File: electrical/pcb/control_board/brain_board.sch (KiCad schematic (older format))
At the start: 6 parts

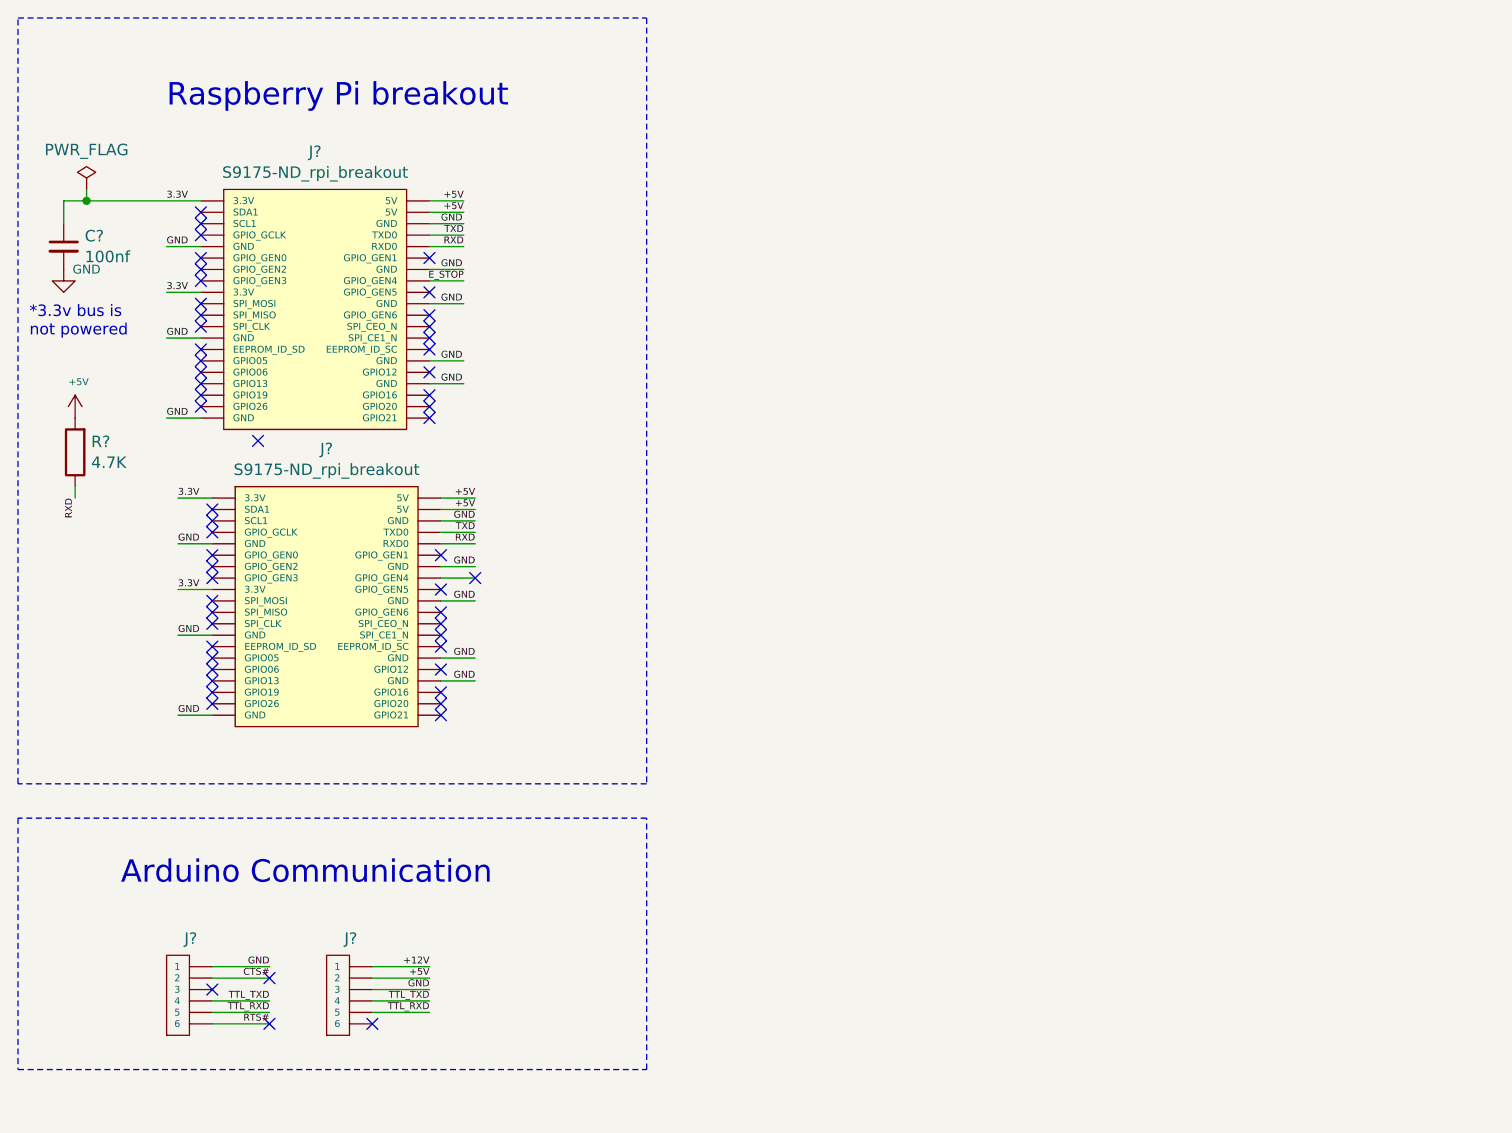
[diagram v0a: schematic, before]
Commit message: add inter board connector
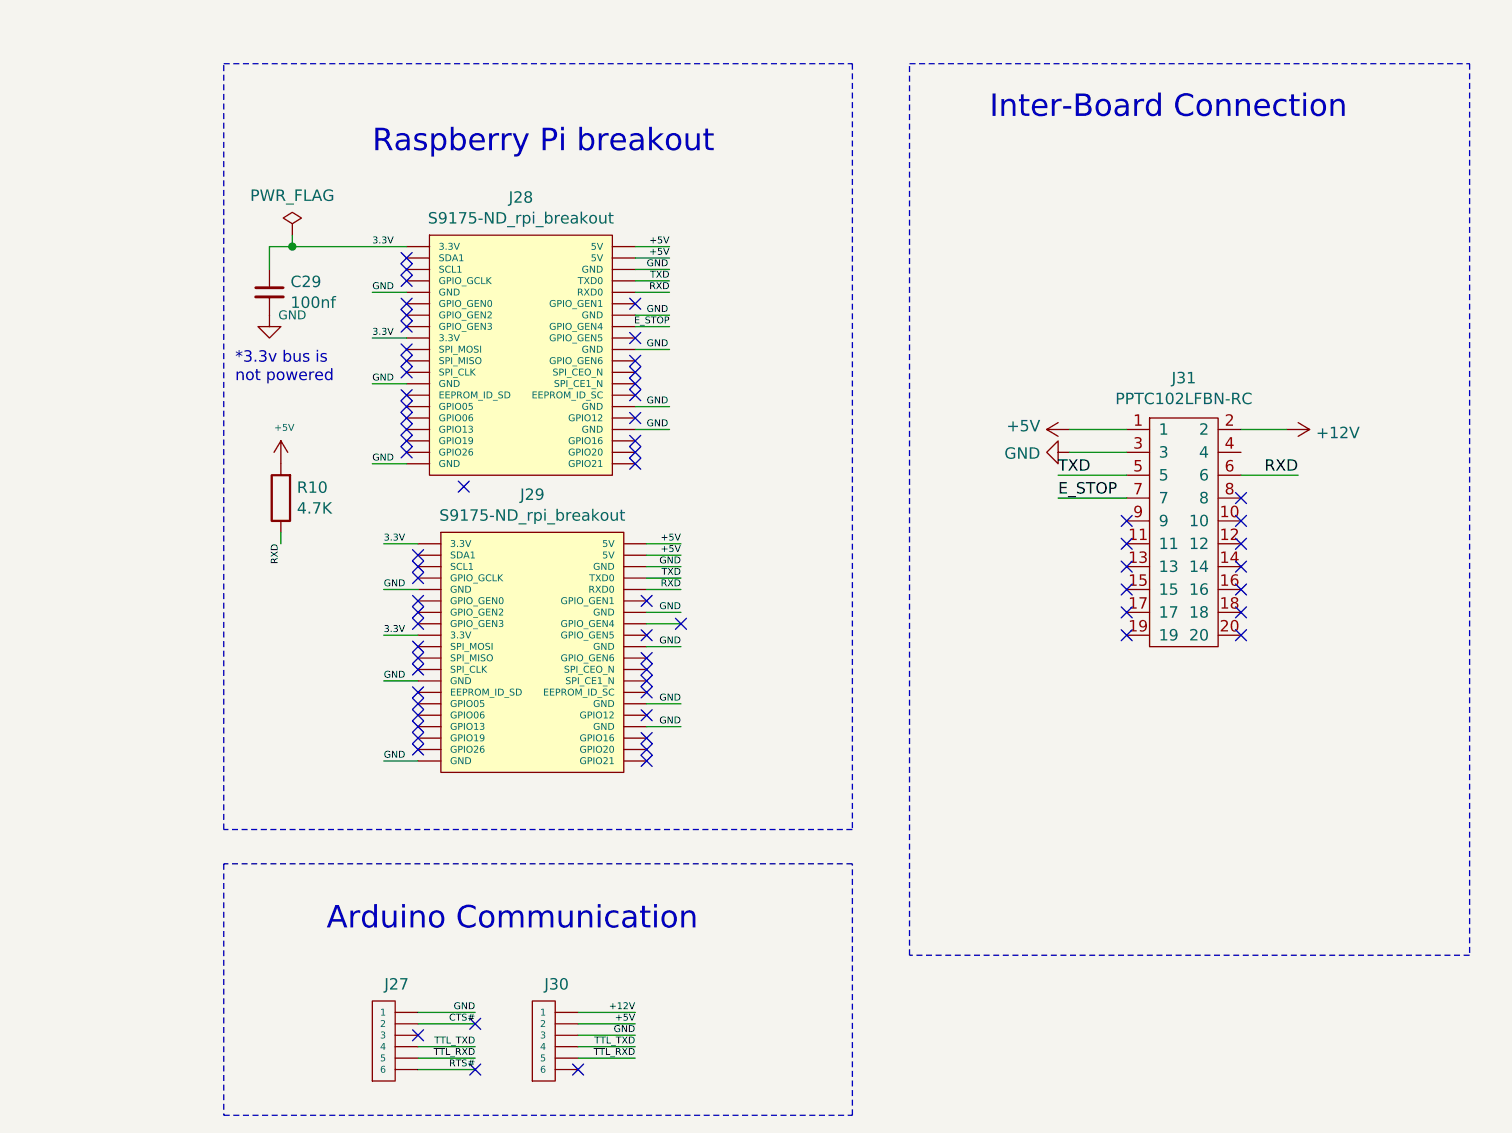
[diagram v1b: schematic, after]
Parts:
- added J31: PPTC102LFBN-RC, symbol JPL_Robotics_Lib:PPTC102LFBN-RC
- gave numbers to parts that had none: 6
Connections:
- wire segments 44 -> 50
- no-connect marks 56 -> 69
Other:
- note added: "Inter-Board Connection"
- moved on the sheet: C29, J27, J28, J29, J30, R10

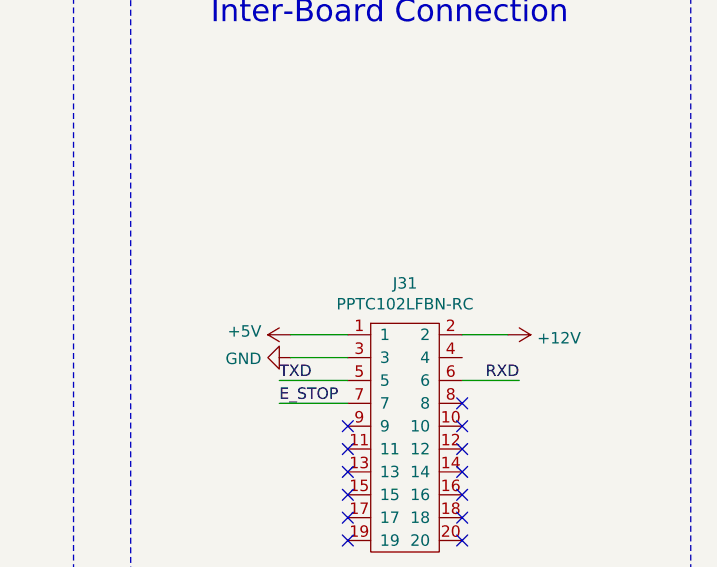
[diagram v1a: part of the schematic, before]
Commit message: moving mounting holes, unnumbering inter board connectors, and adding to kicad readme
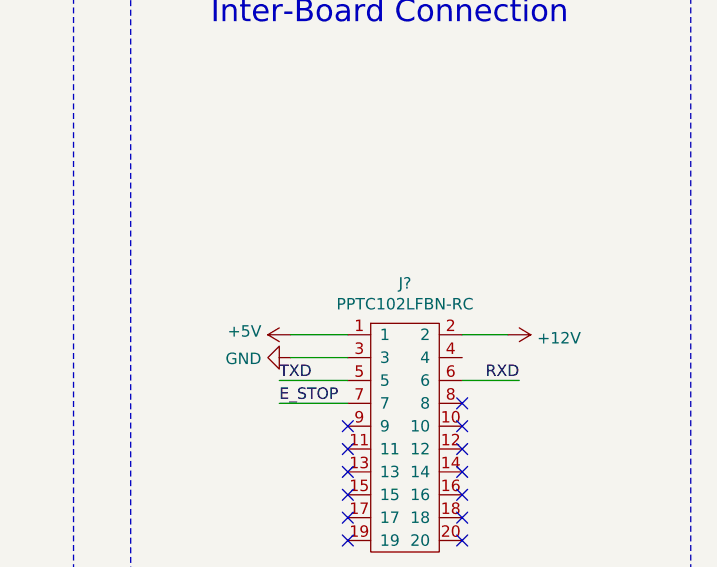
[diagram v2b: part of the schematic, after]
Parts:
- renumbered J31 to J?
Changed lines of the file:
@@
 	7450 3000 7650 3000
 $Comp
-L JPL_Robotics_Lib:PPTC102LFBN-RC J31
+L JPL_Robotics_Lib:PPTC102LFBN-RC J?
 U 1 1 60EE139B
 P 7200 2850
-F 0 "J31" H 7200 2925 50  0000 C CNN
+F 0 "J?" H 7200 2925 50  0000 C CNN
 F 1 "PPTC102LFBN-RC" H 7200 2834 50  0000 C CNN
 F 2 "" H 7500 2850 50  0001 C CNN

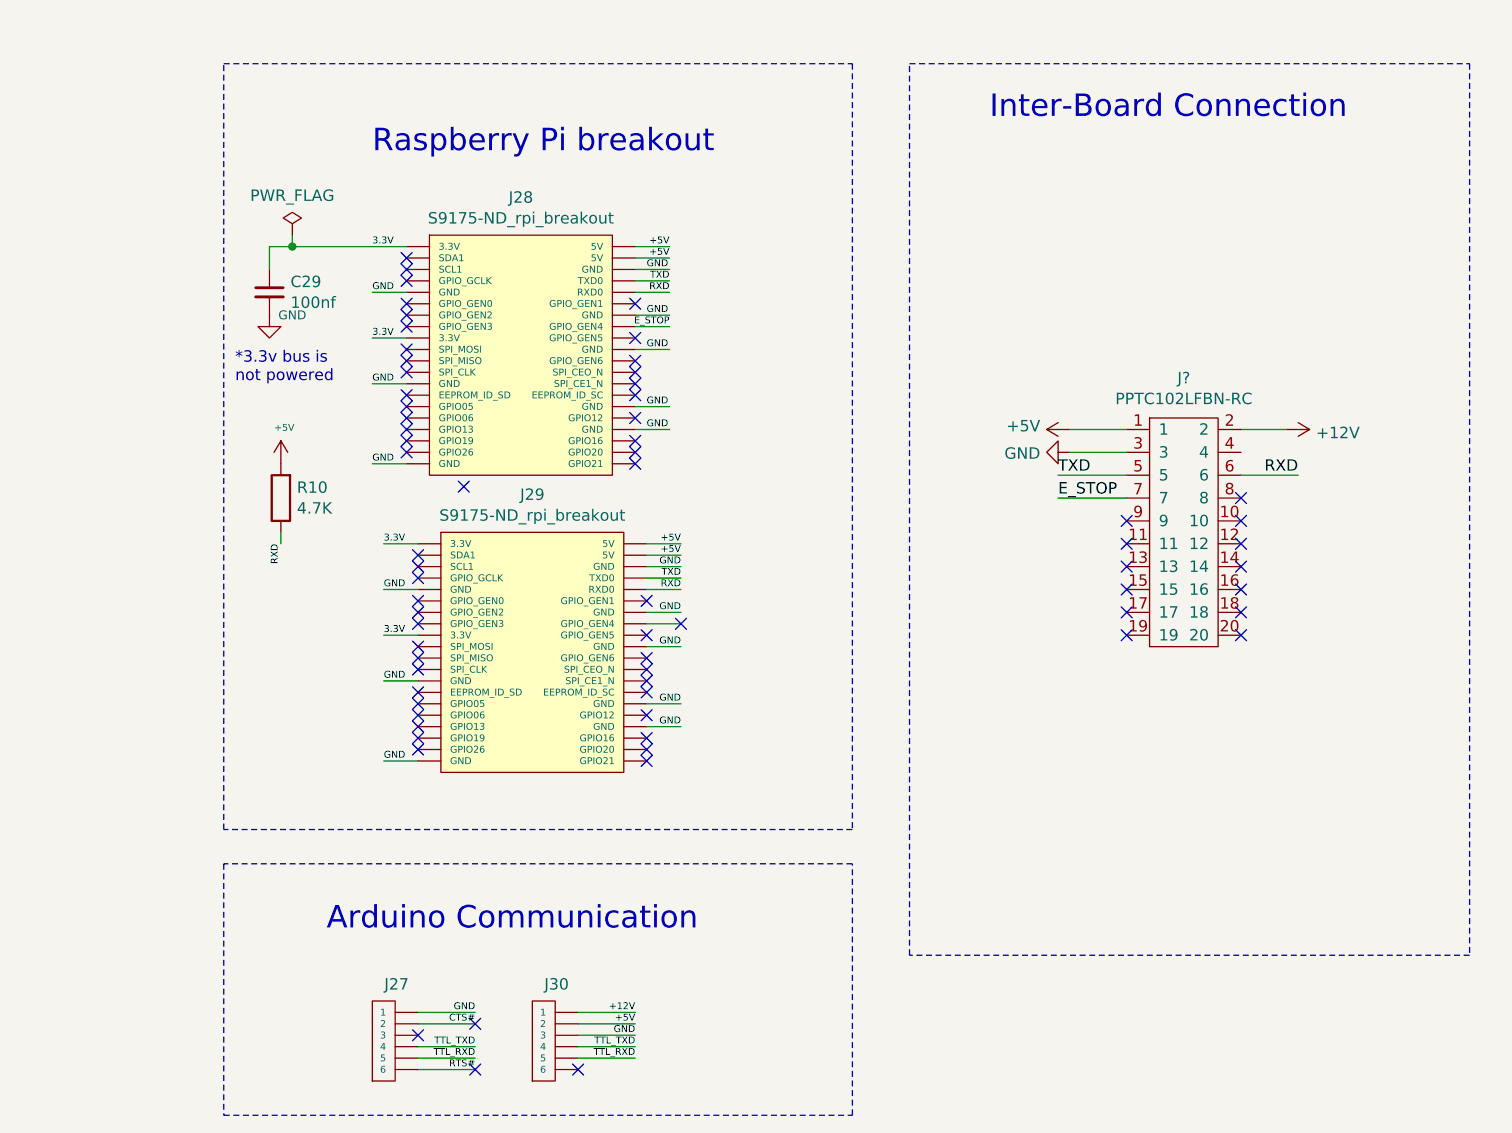
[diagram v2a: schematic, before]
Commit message: Fix numbering to align with component ref designators before splitting into multiple sheets, add numbering for new inter-board connectors
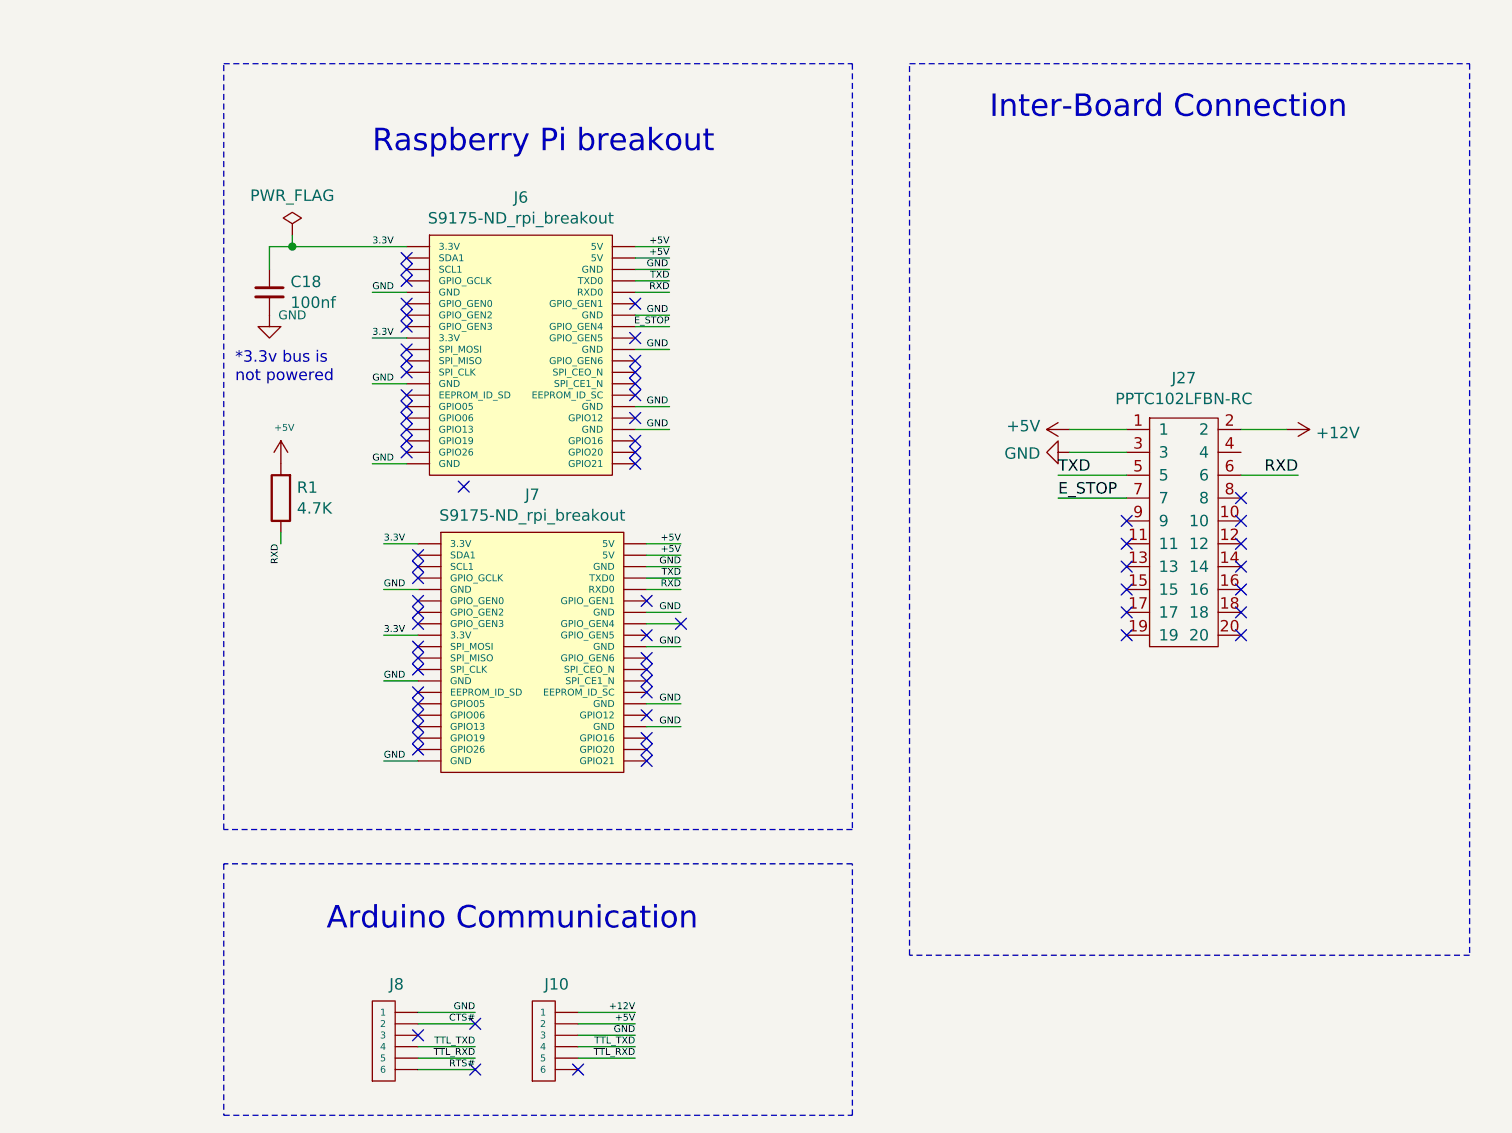
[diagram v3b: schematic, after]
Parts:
- gave numbers to parts that had none: 1
- renumbered C29 to C18, J30 to J10, J28 to J6, J29 to J7, J27 to J8, R10 to R1
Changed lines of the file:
@@
 $EndDescr
 $Comp
-L Device:R R10
+L Device:R R1
 U 1 1 60A8A8D9
 P 3250 3300
-F 0 "R10" H 3180 3254 50  0000 R CNN
+F 0 "R1" H 3180 3254 50  0000 R CNN
 F 1 "4.7K" H 3180 3345 50  0000 R CNN
 F 2 "Resistor_THT:R_Axial_DIN0207_L6.3mm_D2.5mm_P7.62mm_Horizontal" V 3180 3300 50  0001 C CNN
@@
 E_STOP
 $Comp
-L JPL_Robotics_Lib:S9175-ND_rpi_breakout J29
+L JPL_Robotics_Lib:S9175-ND_rpi_breakout J7
 U 1 1 60A8A8FC
 P 3750 4600
-F 0 "J29" H 4350 5915 50  0000 C CNN
+F 0 "J7" H 4350 5915 50  0000 C CNN
 F 1 "S9175-ND_rpi_breakout" H 4350 5824 50  0000 C CNN
 F 2 "JPL Robotics:S9175-ND" H 4000 5850 50  0001 C CNN
@@
 GND
 $Comp
-L JPL_Robotics_Lib:6posheader J27
+L JPL_Robotics_Lib:6posheader J8
 U 1 1 60A8A91E
 P 3650 5850
-F 0 "J27" H 3756 6273 50  0000 C CNN
+F 0 "J8" H 3756 6273 50  0000 C CNN
 F 1 "6posheader" H 3850 6350 50  0001 C CNN
 F 2 "JPL Robotics:6x1 Header Pin 0.1 Pitch" H 3650 5850 50  0001 C CNN
@@
 	3850 5800 4100 5800
 $Comp
-L JPL_Robotics_Lib:6posheader J30
+L JPL_Robotics_Lib:6posheader J10
 U 1 1 60A8A929
 P 4350 5850
-F 0 "J30" H 4456 6273 50  0000 C CNN
+F 0 "J10" H 4456 6273 50  0000 C CNN
 F 1 "6posheader" H 4550 6350 50  0001 C CNN
 F 2 "JPL Robotics:455-1708-ND" H 4350 5850 50  0001 C CNN
@@
 GND
 $Comp
-L Device:C_Small C29
+L Device:C_Small C18
 U 1 1 60A8A94F
 P 3200 2400
-F 0 "C29" H 3292 2446 50  0000 L CNN
+F 0 "C18" H 3292 2446 50  0000 L CNN
 F 1 "100nf" H 3292 2355 50  0000 L CNN
 F 2 "Resistor_THT:R_Axial_DIN0207_L6.3mm_D2.5mm_P7.62mm_Horizontal" H 3200 2400 50  0001 C CNN
@@
 *3.3v bus is \nnot powered
 $Comp
-L JPL_Robotics_Lib:S9175-ND_rpi_breakout J28
+L JPL_Robotics_Lib:S9175-ND_rpi_breakout J6
 U 1 1 60A8A979
 P 3700 3300
-F 0 "J28" H 4300 4615 50  0000 C CNN
+F 0 "J6" H 4300 4615 50  0000 C CNN
 F 1 "S9175-ND_rpi_breakout" H 4300 4524 50  0000 C CNN
 F 2 "JPL Robotics:S9175-ND" H 3950 4550 50  0001 C CNN
@@
 	7450 3000 7650 3000
 $Comp
-L JPL_Robotics_Lib:PPTC102LFBN-RC J?
+L JPL_Robotics_Lib:PPTC102LFBN-RC J27
 U 1 1 60EE139B
 P 7200 2850
-F 0 "J?" H 7200 2925 50  0000 C CNN
+F 0 "J27" H 7200 2925 50  0000 C CNN
 F 1 "PPTC102LFBN-RC" H 7200 2834 50  0000 C CNN
 F 2 "" H 7500 2850 50  0001 C CNN
